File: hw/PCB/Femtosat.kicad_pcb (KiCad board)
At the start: 2 copper layers, 83.8 x 34 mm, 29 parts, among them J1 USB_B_Micro, J2 Programmer, J3 SMA, J4 Battery, U0 AP7215-33YG-13, U1 SAMD21G, U2 TRH-G2, U3 AV4524, U4 RFM69HCW, U5 XA1110, Y1 32.768kHz

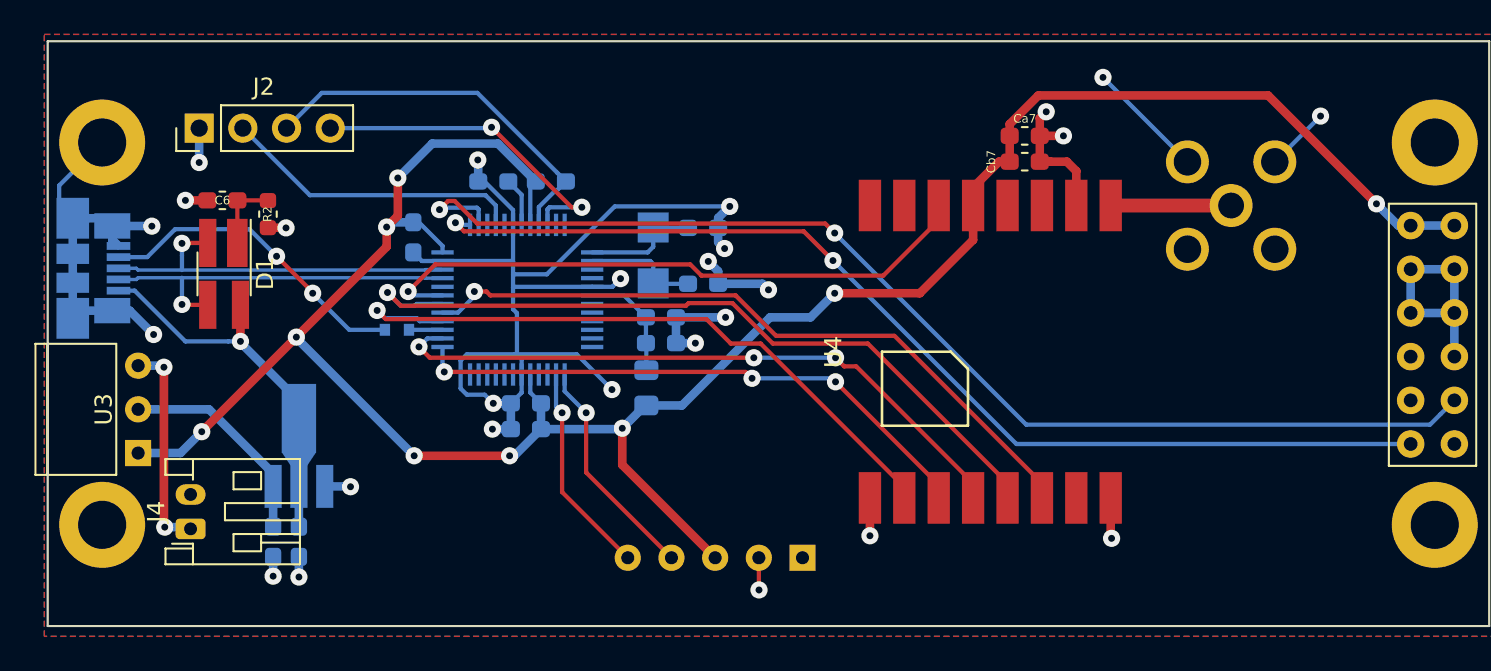
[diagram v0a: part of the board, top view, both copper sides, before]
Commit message: Added more labels in the Silk layer.
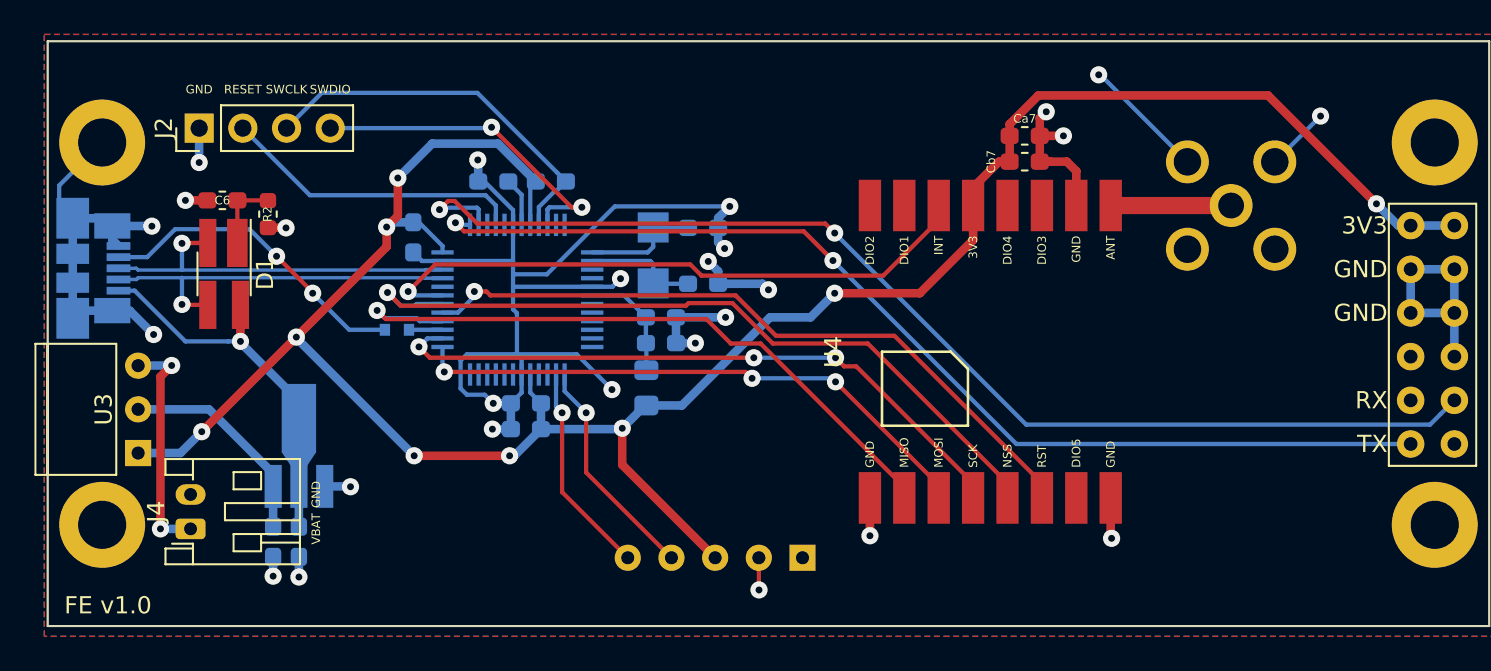
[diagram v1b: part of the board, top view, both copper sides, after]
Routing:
- net /VBAT: track 12.4 -> 13.5 mm
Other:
- board text added: "3V3"
- board text added: "ANT"
- board text added: "DIO1"
- board text added: "DIO2"
- board text added: "DIO3"
- board text added: "DIO4"
- board text added: "DIO5"
- board text added: "FE v1.0"
- board text added: "GND"
- board text added: "INT"
- board text added: "MISO"
- board text added: "MOSI"
- board text added: "NSS"
- board text added: "RESET"
- board text added: "RST"
- board text added: "RX"
- board text added: "SCK"
- board text added: "SCL"
- board text added: "SDA"
- board text added: "SWCLK"
- board text added: "SWDIO"
- board text added: "TX"
- board text added: "VBAT"
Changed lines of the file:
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@@
   (general
     (thickness 1.6)
-    (drawings 4)
+    (drawings 37)
     (tracks 377)
     (zones 0)
@@
     (mod_text_size 1 1)
     (mod_text_width 0.15)
-    (pad_size 5 5)
-    (pad_drill 2.8)
+    (pad_size 1.7 1.7)
+    (pad_drill 1)
     (pad_to_mask_clearance 0.051)
     (solder_mask_min_width 0.25)
@@
       (effects (font (size 0.4 0.4) (thickness 0.04)))
     )
-    (fp_text user %R (at 0 -1.2 90) (layer B.Fab)
+    (fp_text user %R (at 0 -1.2 90) (layer B.Fab) hide
       (effects (font (size 1 1) (thickness 0.15)) (justify mirror))
     )
@@
     (descr "Through hole straight pin header, 1x04, 2.54mm pitch, single row")
     (tags "Through hole pin header THT 1x04 2.54mm single row")
-    (fp_text reference J2 (at 2.4 3.75 180) (layer F.SilkS)
+    (fp_text reference J2 (at 0 -2.05 270) (layer F.SilkS)
       (effects (font (size 1 1) (thickness 0.15)))
     )
@@
     (pad 3 thru_hole circle (at 0 2.54 180) (size 1.524 1.524) (drill 0.762) (layers *.Cu *.Mask)
       (net 52 /VBAT))
+  )
+  (gr_text "FE v1.0" (at 104.7 83.2) (layer F.SilkS)
+    (effects (font (size 1 1) (thickness 0.15)))
+  )
+  (gr_text GND (at 116.8 76.75 90) (layer F.SilkS)
+    (effects (font (size 0.5 0.5) (thickness 0.08)))
+  )
+  (gr_text VBAT (at 116.8 78.75 90) (layer F.SilkS)
+    (effects (font (size 0.5 0.5) (thickness 0.08)))
+  )
+  (gr_text INT (at 145.08 79.2 270) (layer B.SilkS)
+    (effects (font (size 1 1) (thickness 0.15)) (justify left mirror))
+  )
+  (gr_text SCL (at 134.92 79.2 270) (layer B.SilkS)
+    (effects (font (size 1 1) (thickness 0.15)) (justify left mirror))
+  )
+  (gr_text SDA (at 137.46 79.2 270) (layer B.SilkS)
+    (effects (font (size 1 1) (thickness 0.15)) (justify left mirror))
+  )
+  (gr_text 3V3 (at 140 79.2 270) (layer B.SilkS)
+    (effects (font (size 1 1) (thickness 0.15)) (justify left mirror))
+  )
+  (gr_text GND (at 142.54 79.2 90) (layer B.SilkS)
+    (effects (font (size 1 1) (thickness 0.15)) (justify right mirror))
+  )
+  (gr_text TX (at 179.1 73.815) (layer F.SilkS)
+    (effects (font (size 1 1) (thickness 0.15)) (justify right))
+  )
+  (gr_text RX (at 179.1 71.275) (layer F.SilkS)
+    (effects (font (size 1 1) (thickness 0.15)) (justify right))
+  )
+  (gr_text GND (at 179.1 66.195) (layer F.SilkS)
+    (effects (font (size 1 1) (thickness 0.15)) (justify right))
+  )
+  (gr_text GND (at 179.1 63.655) (layer F.SilkS)
+    (effects (font (size 1 1) (thickness 0.15)) (justify right))
+  )
+  (gr_text 3V3 (at 179.1 61.115) (layer F.SilkS)
+    (effects (font (size 1 1) (thickness 0.15)) (justify right))
+  )
+  (gr_text ANT (at 163 61.7 90) (layer F.SilkS)
+    (effects (font (size 0.5 0.5) (thickness 0.08)) (justify right))
+  )
+  (gr_text GND (at 161 61.7 90) (layer F.SilkS)
+    (effects (font (size 0.5 0.5) (thickness 0.08)) (justify right))
+  )
+  (gr_text DIO3 (at 159 61.7 90) (layer F.SilkS)
+    (effects (font (size 0.5 0.5) (thickness 0.08)) (justify right))
+  )
+  (gr_text DIO4 (at 157 61.7 90) (layer F.SilkS)
+    (effects (font (size 0.5 0.5) (thickness 0.08)) (justify right))
+  )
+  (gr_text 3V3 (at 155 61.7 90) (layer F.SilkS)
+    (effects (font (size 0.5 0.5) (thickness 0.08)) (justify right))
+  )
+  (gr_text INT (at 153 61.7 90) (layer F.SilkS)
+    (effects (font (size 0.5 0.5) (thickness 0.08)) (justify right))
+  )
+  (gr_text DIO1 (at 151 61.7 90) (layer F.SilkS)
+    (effects (font (size 0.5 0.5) (thickness 0.08)) (justify right))
+  )
+  (gr_text DIO2 (at 149 61.7 90) (layer F.SilkS)
+    (effects (font (size 0.5 0.5) (thickness 0.08)) (justify right))
+  )
+  (gr_text GND (at 163 75.2 90) (layer F.SilkS)
+    (effects (font (size 0.5 0.5) (thickness 0.08)) (justify left))
+  )
+  (gr_text DIO5 (at 161 75.2 90) (layer F.SilkS)
+    (effects (font (size 0.5 0.5) (thickness 0.08)) (justify left))
+  )
+  (gr_text RST (at 159 75.2 90) (layer F.SilkS)
+    (effects (font (size 0.5 0.5) (thickness 0.08)) (justify left))
+  )
+  (gr_text NSS (at 157 75.2 90) (layer F.SilkS)
+    (effects (font (size 0.5 0.5) (thickness 0.08)) (justify left))
+  )
+  (gr_text SCK (at 155 75.2 90) (layer F.SilkS)
+    (effects (font (size 0.5 0.5) (thickness 0.08)) (justify left))
+  )
+  (gr_text MOSI (at 153 75.2 90) (layer F.SilkS)
+    (effects (font (size 0.5 0.5) (thickness 0.08)) (justify left))
+  )
+  (gr_text MISO (at 151 75.2 90) (layer F.SilkS)
+    (effects (font (size 0.5 0.5) (thickness 0.08)) (justify left))
+  )
+  (gr_text GND (at 149 75.2 90) (layer F.SilkS)
+    (effects (font (size 0.5 0.5) (thickness 0.08)) (justify left))
+  )
+  (gr_text SWDIO (at 117.62 53.2) (layer F.SilkS)
+    (effects (font (size 0.5 0.5) (thickness 0.08)))
+  )
+  (gr_text SWCLK (at 115.08 53.2) (layer F.SilkS)
+    (effects (font (size 0.5 0.5) (thickness 0.08)))
+  )
+  (gr_text RESET (at 112.54 53.2) (layer F.SilkS)
+    (effects (font (size 0.5 0.5) (thickness 0.08)))
+  )
+  (gr_text GND (at 110 53.2) (layer F.SilkS)
+    (effects (font (size 0.5 0.5) (thickness 0.08)))
   )
   (gr_line (start 101.2 84.4) (end 101.2 50.4) (layer Edge.Cuts) (width 0.05))
@@
   (via (at 175.2 54.75) (size 1) (drill 0.4) (layers F.Cu B.Cu) (net 2))
   (segment (start 172.54 57.41) (end 175.2 54.75) (width 0.25) (layer B.Cu) (net 2))
-  (via (at 162.55 52.5) (size 1) (drill 0.4) (layers F.Cu B.Cu) (net 2))
-  (segment (start 167.46 57.41) (end 162.55 52.5) (width 0.25) (layer B.Cu) (net 2))
+  (via (at 162.3 52.35) (size 1) (drill 0.4) (layers F.Cu B.Cu) (net 2))
+  (segment (start 167.46 57.41) (end 162.4 52.35) (width 0.25) (layer B.Cu) (net 2))
+  (segment (start 162.4 52.35) (end 162.3 52.35) (width 0.25) (layer B.Cu) (net 2))
   (segment (start 128.75 59.325) (end 127.975 58.55) (width 0.25) (layer B.Cu) (net 3))
   (segment (start 128.75 61.075) (end 128.75 59.325) (width 0.25) (layer B.Cu) (net 3))
@@
   (segment (start 123.725001 63.374999) (end 138.553997 63.374999) (width 0.25) (layer F.Cu) (net 49))
   (segment (start 122.15 64.95) (end 123.725001 63.374999) (width 0.25) (layer F.Cu) (net 49))
-  (via (at 107.95 69.35) (size 1) (drill 0.4) (layers F.Cu B.Cu) (net 52))
-  (segment (start 106.45 69.26) (end 107.86 69.26) (width 0.5) (layer B.Cu) (net 52))
-  (segment (start 107.86 69.26) (end 107.95 69.35) (width 0.5) (layer B.Cu) (net 52))
-  (via (at 108 78.65) (size 1) (drill 0.4) (layers F.Cu B.Cu) (net 52))
-  (segment (start 107.95 69.35) (end 107.95 78.6) (width 0.5) (layer F.Cu) (net 52))
-  (segment (start 107.95 78.6) (end 108 78.65) (width 0.5) (layer F.Cu) (net 52))
-  (segment (start 109.4 78.65) (end 109.5 78.75) (width 0.5) (layer B.Cu) (net 52))
-  (segment (start 108 78.65) (end 109.4 78.65) (width 0.5) (layer B.Cu) (net 52))
-  (segment (start 163 59.95) (end 170 59.95) (width 0.8) (layer F.Cu) (net 53))
+  (via (at 107.75 78.75) (size 1) (drill 0.4) (layers F.Cu B.Cu) (net 52))
+  (segment (start 109.5 78.75) (end 107.75 78.75) (width 0.5) (layer B.Cu) (net 52))
+  (via (at 108.4 69.25) (size 1) (drill 0.4) (layers F.Cu B.Cu) (net 52))
+  (segment (start 107.75 78.75) (end 107.75 69.9) (width 0.5) (layer F.Cu) (net 52))
+  (segment (start 107.75 69.9) (end 108.4 69.25) (width 0.5) (layer F.Cu) (net 52))
+  (segment (start 106.46 69.25) (end 106.45 69.26) (width 0.5) (layer B.Cu) (net 52))
+  (segment (start 108.4 69.25) (end 106.46 69.25) (width 0.5) (layer B.Cu) (net 52))
+  (segment (start 163 59.95) (end 170 59.95) (width 1) (layer F.Cu) (net 53))
   (segment (start 114.3 75.53) (end 114.3 76.28) (width 0.5) (layer B.Cu) (net 54))
   (segment (start 110.57 71.8) (end 114.3 75.53) (width 0.5) (layer B.Cu) (net 54))

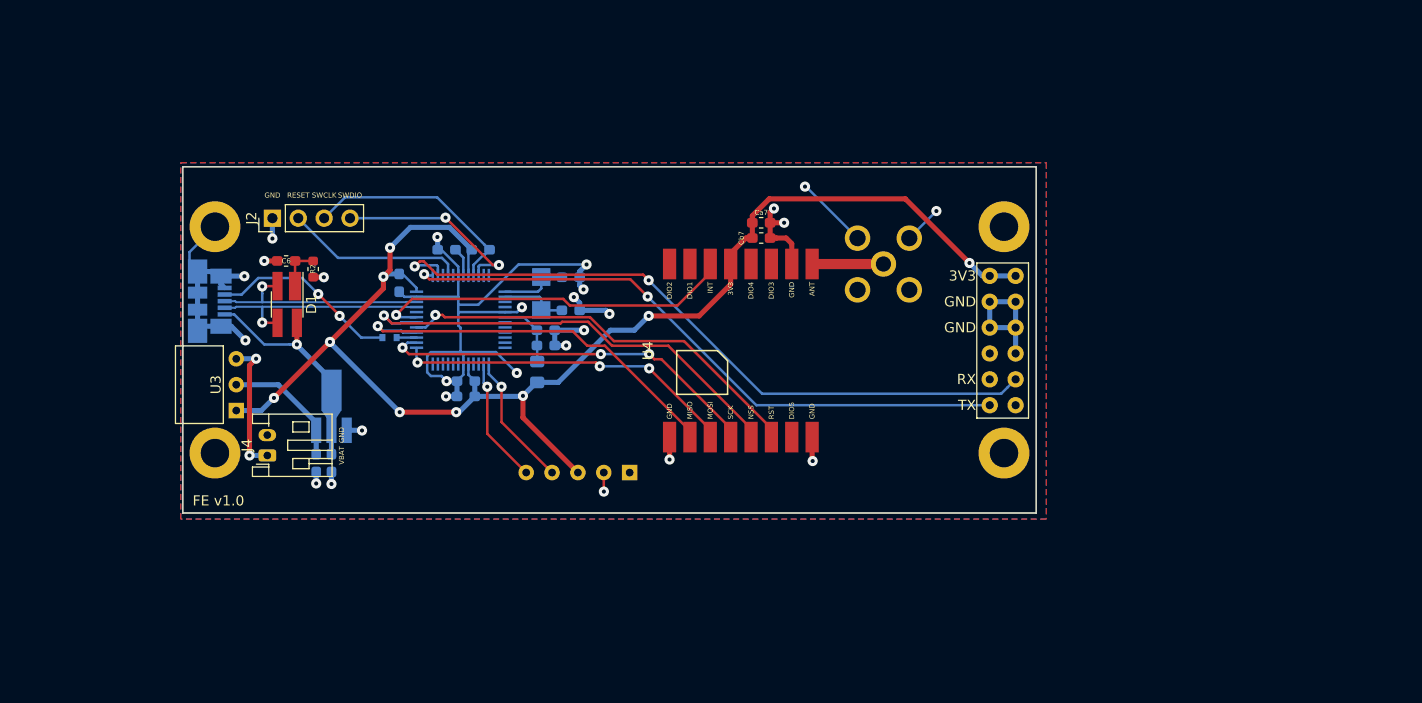
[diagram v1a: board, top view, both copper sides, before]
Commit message: Started the new design of the PCB's layout.
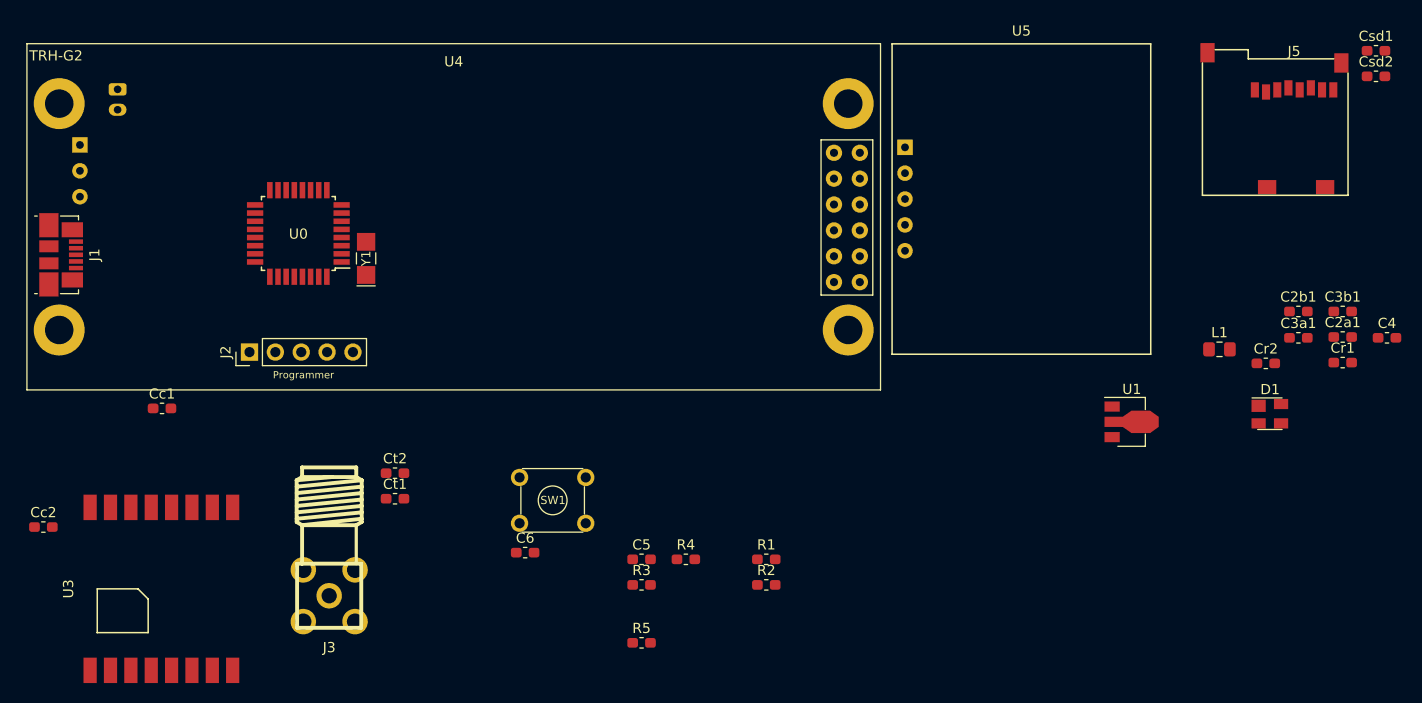
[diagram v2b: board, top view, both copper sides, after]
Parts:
- removed Ca7, Cb7: C, Capacitor_SMD:C_0603_1608Metric_Pad1.05x0.95mm_HandSolder
- removed D3: D_Schottky, Diode_SMD:D_SOD-523
- added Csd1: 10uF, Capacitor_SMD:C_0603_1608Metric_Pad1.05x0.95mm_HandSolder, F.Cu at (218.4, 39.0)
- added Csd2: 100nF, Capacitor_SMD:C_0603_1608Metric_Pad1.05x0.95mm_HandSolder, F.Cu at (218.4, 41.5)
- added Ct1: 0.1uF, Capacitor_SMD:C_0603_1608Metric_Pad1.05x0.95mm_HandSolder, F.Cu at (122.0, 83.0)
- added Ct2: 10uF, Capacitor_SMD:C_0603_1608Metric_Pad1.05x0.95mm_HandSolder, F.Cu at (122.0, 80.5)
- added J5: Micro_SD_Card_Det, SD:microSD_socket, F.Cu at (210.3, 51.7)
- added R3: 1M, Resistor_SMD:R_0603_1608Metric_Pad1.05x0.95mm_HandSolder, F.Cu at (146.2, 91.5)
- added R4: 330, Resistor_SMD:R_0603_1608Metric_Pad1.05x0.95mm_HandSolder, F.Cu at (150.6, 89.0)
- added R5: 100k, Resistor_SMD:R_0603_1608Metric_Pad1.05x0.95mm_HandSolder, F.Cu at (146.2, 97.2)
- added SW1: Reset_push, Button_Switch_THT:SW_TH_Tactile_Omron_B3F-10xx, F.Cu at (134.3, 80.9)
- C2a1, C2b1, C3a1, C3b1, Cc1, Cc2, Cr1, Cr2, J1, J3, L1, R1, U5, Y1: moved to F.Cu
- C4: value 10uF -> 1uF; moved to F.Cu
- C5: value 1uF -> 4.7nF; moved to F.Cu
- C6: value 4.7nF -> 100nF
- D1: footprint Package_TO_SOT_SMD:SOT-143_Handsoldering -> Package_TO_SOT_SMD:SOT-143
- J2: footprint Connector_PinHeader_2.54mm:PinHeader_1x04_P2.54mm_Vertical -> Connector_PinHeader_2.54mm:PinHeader_1x05_P2.54mm_Vertical
- J4: moved to B.Cu
- R2: value 1M -> 10k; footprint Resistor_SMD:R_0603_1608Metric -> Resistor_SMD:R_0603_1608Metric_Pad1.05x0.95mm_HandSolder
- U0: value AP7215-33YG-13 -> SAMD21E; footprint Package_TO_SOT_SMD:SOT-89-3_Handsoldering -> Package_QFP:TQFP-32_7x7mm_P0.8mm; moved to F.Cu
- U1: value SAMD21G -> AP7215-33YG-13; footprint Package_QFP:TQFP-48_7x7mm_P0.5mm -> Package_TO_SOT_SMD:SOT-89-3; moved to F.Cu
- U2: value TRH-G2 -> AV4524; footprint GPS:TRH-G2 -> Interrupt:AV4524; moved to B.Cu
- U3: value AV4524 -> RFM69HCW; footprint Interrupt:AV4524 -> Transceptor:RFM69HCW
- U4: value RFM69HCW -> TRH-G2; footprint Transceptor:RFM69HCW -> GPS:TRH-G2
- moved Cr1 99.8 mm to (215.1, 69.6), turned to 0 degrees
- moved D1 97.1 mm to (207.9, 74.7), turned to 0 degrees
- moved Cr2 93.8 mm to (207.6, 69.7), turned to 0 degrees
- moved C3b1 92.7 mm to (215.1, 64.6), turned to 0 degrees
- moved C4 90.6 mm to (219.4, 67.2), turned to 0 degrees
- moved C3a1 81.9 mm to (210.8, 67.2), turned to 0 degrees
- moved C2a1 78.3 mm to (215.1, 67.1)
- moved C2b1 74.0 mm to (210.8, 64.6)
- moved L1 67.0 mm to (203.0, 68.3), turned to 0 degrees
- moved U1 66.2 mm to (193.9, 75.5), turned to 0 degrees
- moved J3 63.4 mm to (115.6, 92.5), turned to 0 degrees
- moved Cc2 56.0 mm to (87.5, 85.8)
- moved U2 54.6 mm to (91.1, 50.8), turned to 180 degrees
- moved R2 54.2 mm to (158.5, 91.5), turned to 0 degrees
- moved U5 46.2 mm to (183.6, 53.6), turned to 0 degrees
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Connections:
- C3a1 pad 1: /3V3 -> +3V3
- C3b1 pad 1: /3V3 -> +3V3
- C4 pad 1: /3V3 -> /VDDCORE
- C5 pad 1: /VDDCORE -> /USB/SHIELD
- C6 pad 1: Net-(C6-Pad1) -> /RESET
- Cr1 pad 1: /VBUS -> /Power/VIN
- Cr2 pad 1: /Power/REG_USB -> +3V3
- D1 pad 1: Net-(C6-Pad1) -> /USB/SHIELD
- D1 pad 4: /VBUS -> /VUSB
- J1 pad 1: /VBUS -> /VUSB
- J1 pad 6: GND -> /USB/SHIELD
- J2 pad 1: GND -> /RESET
- J2 pad 2: /RESET -> +3V3
- J2 pad 3: /SWCLK -> GND
- J2 pad 4: /SWDIO -> /SWCLK
- L1 pad 2: /3V3 -> +3V3
- R1 pad 1: /3V3 -> +3V3
- R2 pad 1: Net-(C6-Pad1) -> +3V3
- R2 pad 2: GND -> /RESET
- U0 pad 1: GND -> /XIN32
- U0 pad 2: /VBUS -> /XOUT32
- U0 pad 3: /Power/REG_USB -> Net-(U0-Pad3)
- U1 pad 1: /XIN32 -> GND
- U1 pad 2: /XOUT32 -> /Power/VIN
- U1 pad 3: /A0 -> +3V3
- U2 pad 1: /3V3 -> /Power/VIN
- U2 pad 2: /3V3 -> /VUSB
- U2 pad 3: GND -> /VBAT
- U3 pad 1: /3V3 -> GND
- U3 pad 2: /Power/REG_USB -> /MISO
- U3 pad 3: /VBAT -> /MOSI
- U4 pad 1: GND -> +3V3
- U4 pad 10: GND -> /RX
- U4 pad 11: /Communication/DIO3 -> /TX
- U4 pad 12: /Communication/DIO4 -> Net-(U4-Pad12)
- U4 pad 2: /MISO -> +3V3
- U4 pad 3: /MOSI -> GND
- U4 pad 4: /SCK -> GND
- U4 pad 5: /TRX_NSS -> GND
- U4 pad 6: /TRX_RST -> GND
- U4 pad 7: /Communication/DIO5 -> Net-(U4-Pad7)
- U4 pad 9: /Communication/ANT -> Net-(U4-Pad9)
- U5 pad 1: Net-(U5-Pad1) -> /GPS_INT
- U5 pad 3: /3V3 -> +3V3
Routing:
- net GND: track 143.0 -> 0.00 mm, vias 26 -> 0
- net /3V3: track 138.7 -> 0.00 mm, vias 9 -> 0
- net /RX: track 68.4 -> 0.00 mm, vias 2 -> 0
- net /TX: track 61.8 -> 0.00 mm, vias 2 -> 0
- net /TRX_NSS: track 45.2 -> 0.00 mm, vias 1 -> 0
- net /TRX_RST: track 41.0 -> 0.00 mm, vias 1 -> 0
- net /MISO: track 39.6 -> 0.00 mm, vias 1 -> 0
- net /SCK: track 37.9 -> 0.00 mm, vias 3 -> 0
- net /TRX_INT: track 36.1 -> 0.00 mm, vias 1 -> 0
- net /MOSI: track 33.7 -> 0.00 mm, vias 3 -> 0
- net /VBUS: track 22.6 -> 0.00 mm, vias 1 -> 0
- net /SWCLK: track 22.5 -> 0.00 mm
- net /USB_P: track 22.0 -> 0.00 mm, vias 1 -> 0
- net /USB_N: track 22.0 -> 0.00 mm, vias 1 -> 0
- net /SWDIO: track 19.5 -> 0.00 mm, vias 2 -> 0
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- removed copper zone on B.Cu, net GND
- removed copper zone on F.Cu, net GND
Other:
- board outline removed
- net class Default: trace_width 0.25 -> 0.55; via_dia 1 -> 1.6; via_drill 0.4 -> 0.7
- net class Power: trace_width 0.5 -> 0.8; via_dia 1 -> 1.6; via_drill 0.4 -> 0.7
- net class USB added: clearance 0.2, trace_width 0.45, via_dia 1.6, via_drill 0.7
- net class uC: trace_width 0.25 -> 0.55; via_dia 1 -> 1.6; via_drill 0.4 -> 0.7
- board text removed: "3V3"
- board text removed: "ANT"
- board text removed: "DIO1"
- board text removed: "DIO2"
- board text removed: "DIO3"
- board text removed: "DIO4"
- board text removed: "DIO5"
- board text removed: "FE v1.0"
- board text removed: "GND"
- board text removed: "INT"
- board text removed: "MISO"
- board text removed: "MOSI"
- board text removed: "NSS"
- board text removed: "RESET"
- board text removed: "RST"
- board text removed: "RX"
- board text removed: "SCK"
- board text removed: "SCL"
- board text removed: "SDA"
- board text removed: "SWCLK"
- board text removed: "SWDIO"
- board text removed: "TX"
- board text removed: "VBAT"
